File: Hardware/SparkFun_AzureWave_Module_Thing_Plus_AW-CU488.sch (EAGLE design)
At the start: 59 parts, among them J1 THING_PLUS, J3 QWIIC_RA, J5 USB-C, Q1 3.1A/30V/105mΩ, Q2 MBT3904DW1T1, U2 CP210X, U3 AP2112K-3.3V, U4 MCP73831

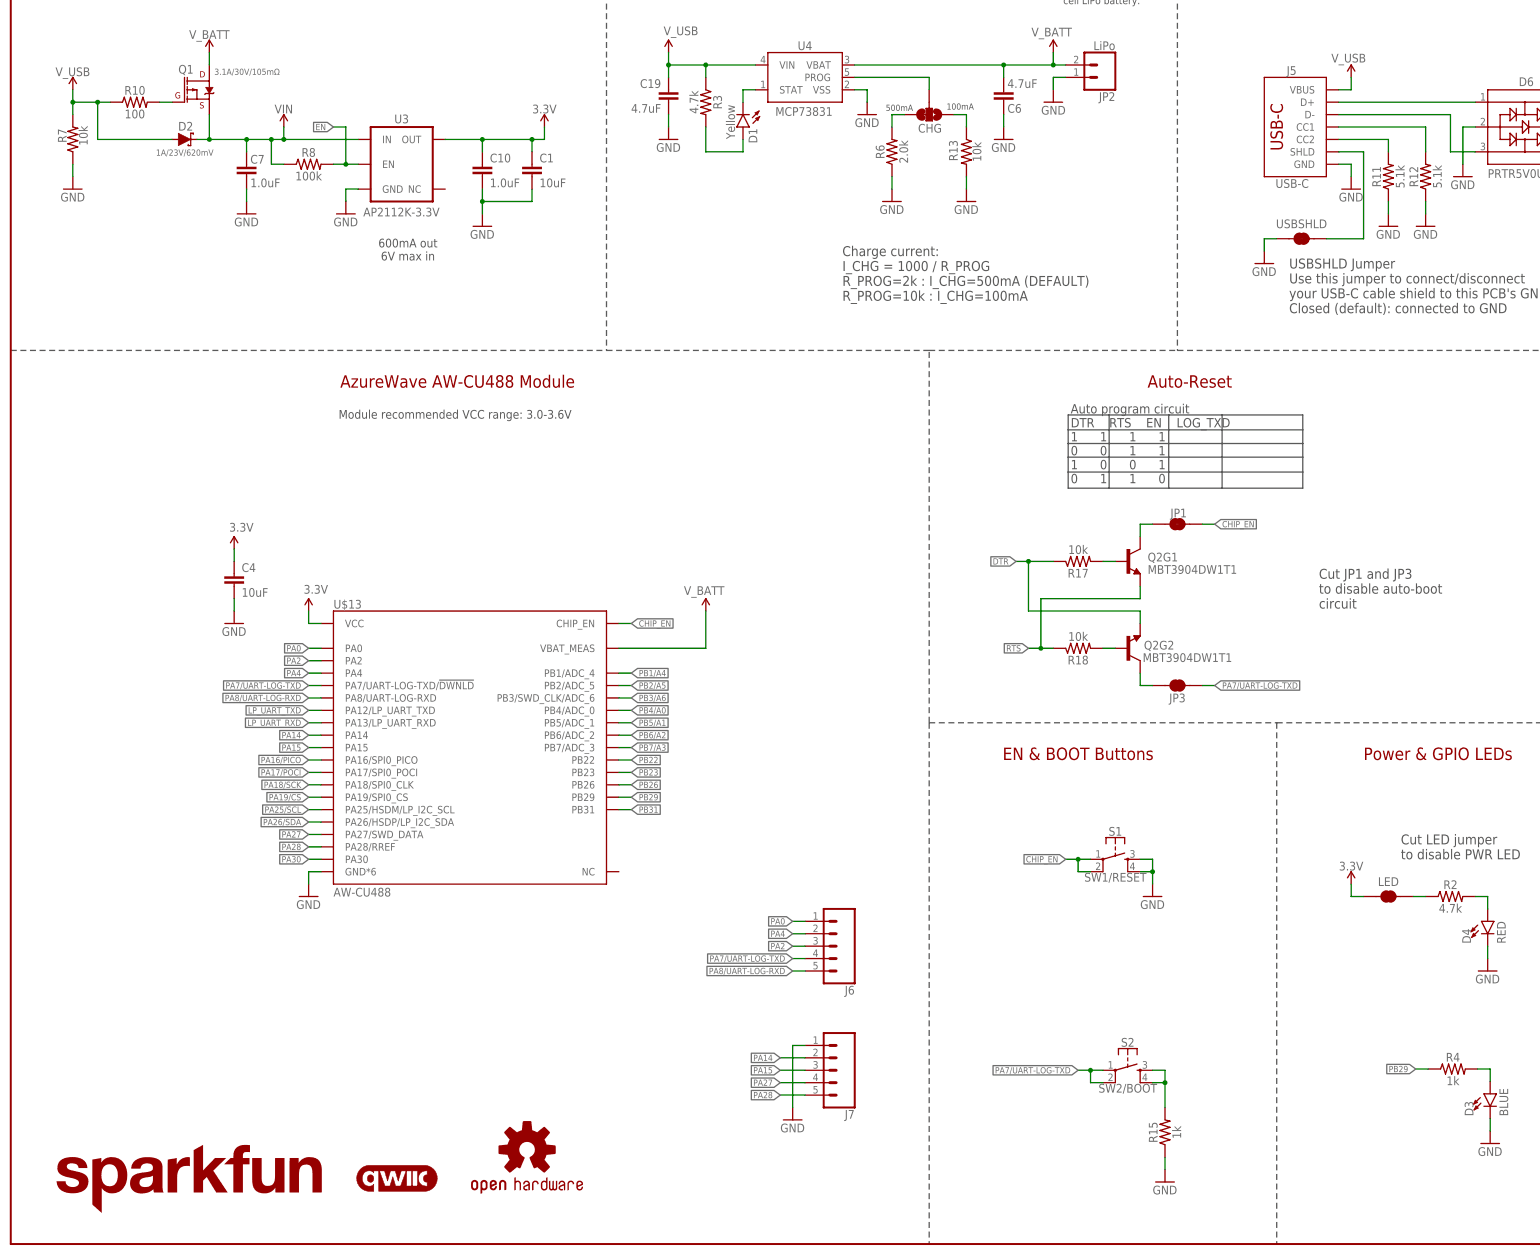
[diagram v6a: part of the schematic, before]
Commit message: more changes from reds review
-auto-reset disable jumpers changed to JP1 and JP2
-added more measures to top pht header on header rows
-swapped vreg from ap2112 to XC6222
-Add SFE LOGO to bottom silk
-more gnd vias near potential gnd loops
-fixed acid traps
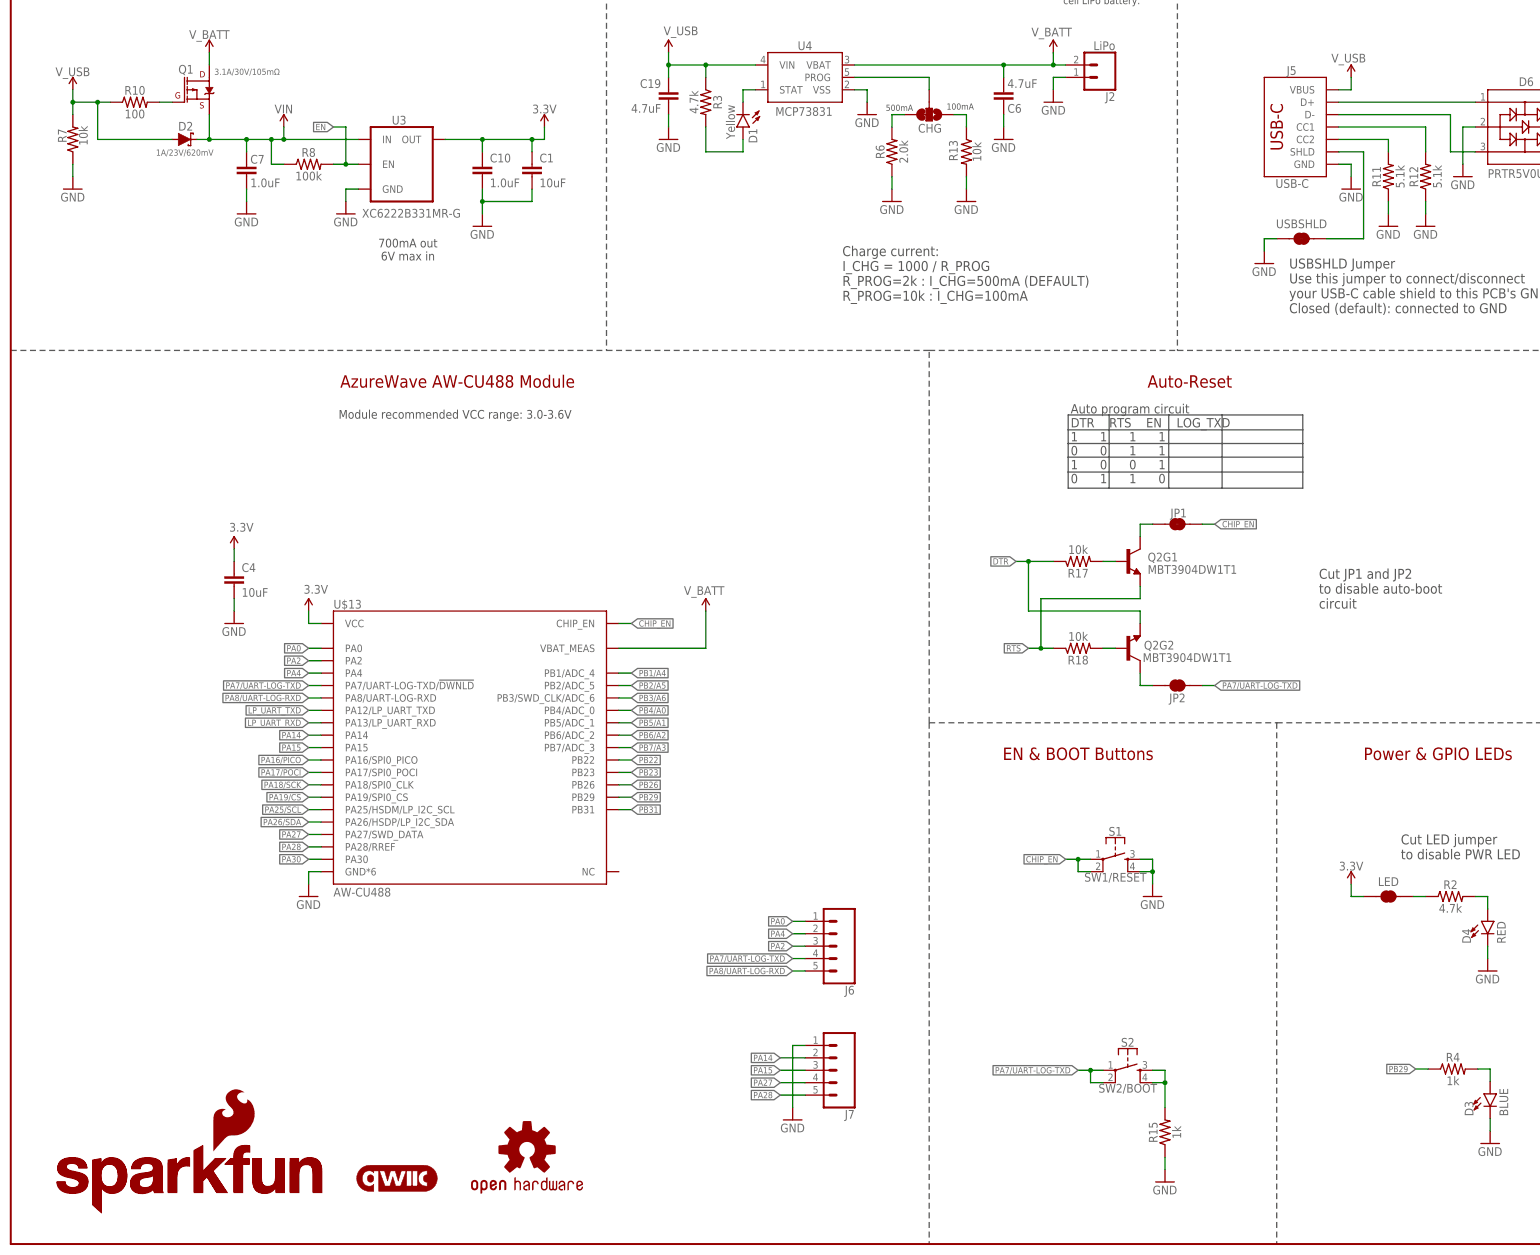
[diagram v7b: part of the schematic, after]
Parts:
- removed JP3: JUMPER-SMT_2_NC_TRACE_SILK, SparkFun-Jumpers:JUMPER-SMT_2_NC_TRACE_SILK
- added J2: LiPo, SparkFun-Connectors:CONN_02-JST-2MM-SMT
- added LOGO3: SFE_LOGO_NAME_FLAME.1_INCH, SparkFun-Aesthetics:SFE_LOGO_NAME_FLAME.1_INCH
- JP2: value LiPo -> JUMPER-SMT_2_NC_TRACE_SILK; device SparkFun-Connectors:CONN_02-JST-2MM-SMT -> SparkFun-Jumpers:JUMPER-SMT_2_NC_TRACE_SILK
- U3: value AP2112K-3.3V -> XC6222B331MR-G; device SparkFun-IC-Power:V_REG_AP2112K-3.3V -> SparkFun-IC-Power:XC6222B331MR-G
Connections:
- net GND: now also J2.2; no longer JP2.2
- net N$10: now also JP2.1; no longer JP3.1
- net PA7/UART-LOG-TXD: now also JP2.2; no longer JP3.2
- net V_BATT: now also J2.1; no longer JP2.1
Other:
- note added: "700mA out 6V max in"
- note added: "Cut JP1 and JP2 to disable auto-boot circuit"
- note removed: "600mA out 6V max in"
- note removed: "Cut JP1 and JP3 to disable auto-boot circuit"
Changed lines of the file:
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@@
 <part name="R7" library="SparkFun-Resistors" deviceset="10KOHM" device="-0402T-1/16W-1%" value="10k"/>
 <part name="GND13" library="SparkFun-PowerSymbols" deviceset="GND" device=""/>
-<part name="JP2" library="SparkFun-Connectors" deviceset="CONN_02" device="-JST-2MM-SMT" value="LiPo"/>
+<part name="J2" library="SparkFun-Connectors" deviceset="CONN_02" device="-JST-2MM-SMT" value="LiPo"/>
 <part name="GND4" library="SparkFun-PowerSymbols" deviceset="GND" device=""/>
 <part name="D1" library="SparkFun-LED" deviceset="LED-YELLOW" device="0603" value="Yellow"/>
 <part name="R3" library="SparkFun-Resistors" deviceset="4.7KOHM" device="-0402T-1/16W-1%" value="4.7k"/>
-<part name="U3" library="SparkFun-IC-Power" deviceset="V_REG_AP2112" device="K-3.3V" value="AP2112K-3.3V">
+<part name="U3" library="SparkFun-IC-Power" deviceset="XC6222" device="B331MR-G" value="XC6222B331MR-G">
 <attribute name="PROD_ID" value="VREG-12457"/>
 </part>
@@
 <part name="GND22" library="SparkFun-PowerSymbols" deviceset="GND" device=""/>
 <part name="JP1" library="SparkFun-Jumpers" deviceset="JUMPER-SMT_2_NC_TRACE" device="_SILK" package3d_urn="urn:adsk.eagle:package:39281/1" value=""/>
-<part name="JP3" library="SparkFun-Jumpers" deviceset="JUMPER-SMT_2_NC_TRACE" device="_SILK" package3d_urn="urn:adsk.eagle:package:39281/1" value=""/>
+<part name="JP2" library="SparkFun-Jumpers" deviceset="JUMPER-SMT_2_NC_TRACE" device="_SILK" package3d_urn="urn:adsk.eagle:package:39281/1" value=""/>
 <part name="LOGO1" library="SparkFun-Aesthetics" deviceset="SFE_LOGO_NAME" device=".1_INCH"/>
+<part name="LOGO3" library="SparkFun-Aesthetics" deviceset="SFE_LOGO_NAME_FLAME" device=".1_INCH"/>
 </parts>
 <sheets>
@@
 <text x="60.96" y="271.78" size="2.54" layer="94" font="vector" align="bottom-center">Voltage Regulator</text>
 <text x="177.8" y="271.78" size="2.54" layer="94" font="vector" align="bottom-center">Lithium-Polymer Battery Charger (1-cell)</text>
-<text x="81.28" y="205.74" size="1.778" layer="97" font="vector" align="top-center">600mA out
+<text x="81.28" y="205.74" size="1.778" layer="97" font="vector" align="top-center">700mA out
 6V max in</text>
 <wire x1="0" y1="182.88" x2="121.92" y2="182.88" width="0.2032" layer="97" style="longdash"/>
@@
 your USB-C cable shield to this PCB's GND.
 Closed (default): connected to GND</text>
-<text x="267.716" y="130.048" size="2.032" layer="97" font="vector" rot="MR180" align="top-left">Cut JP1 and JP3
+<text x="267.716" y="130.048" size="2.032" layer="97" font="vector" rot="MR180" align="top-left">Cut JP1 and JP2
 to disable auto-boot
 circuit</text>
@@
 <attribute name="VALUE" x="10.16" y="213.36" size="1.778" layer="96" font="vector"/>
 </instance>
-<instance part="JP2" gate="G$1" x="223.52" y="241.3" smashed="yes" rot="R180">
+<instance part="J2" gate="G$1" x="223.52" y="241.3" smashed="yes" rot="R180">
 <attribute name="VALUE" x="226.06" y="246.126" size="1.778" layer="96" font="vector" rot="R180"/>
 <attribute name="NAME" x="226.06" y="235.712" size="1.778" layer="95" font="vector" rot="R180"/>
@@
 <instance part="U3" gate="G$1" x="81.28" y="220.98" smashed="yes">
 <attribute name="PROD_ID" x="81.28" y="220.98" size="1.778" layer="96" display="off"/>
-<attribute name="NAME" x="78.486" y="229.362" size="1.778" layer="95" font="vector"/>
-<attribute name="VALUE" x="72.136" y="210.312" size="1.778" layer="96" font="vector"/>
+<attribute name="NAME" x="77.978" y="229.108" size="1.778" layer="95" font="vector"/>
+<attribute name="VALUE" x="71.882" y="211.836" size="1.778" layer="96" font="vector" align="top-left"/>
 </instance>
 <instance part="Q1" gate="G$1" x="38.1" y="236.22" smashed="yes">
@@
 <attribute name="VALUE" x="238.76" y="144.272" size="1.778" layer="96" font="vector" align="center"/>
 </instance>
-<instance part="JP3" gate="G$1" x="238.76" y="114.3" smashed="yes">
+<instance part="JP2" gate="G$1" x="238.76" y="114.3" smashed="yes">
 <attribute name="NAME" x="238.76" y="111.76" size="1.778" layer="95" font="vector" align="center"/>
 <attribute name="VALUE" x="238.76" y="111.252" size="1.778" layer="96" font="vector" align="center"/>
 </instance>
 <instance part="LOGO1" gate="G$1" x="7.366" y="6.35" smashed="yes"/>
+<instance part="LOGO3" gate="G$1" x="8.636" y="5.842" smashed="yes"/>
 </instances>
 <busses>
@@
 <pinref part="GND4" gate="1" pin="GND"/>
 <wire x1="213.36" y1="238.76" x2="213.36" y2="236.22" width="0.1524" layer="91"/>
-<pinref part="JP2" gate="G$1" pin="2"/>
+<pinref part="J2" gate="G$1" pin="2"/>
 <wire x1="213.36" y1="238.76" x2="215.9" y2="238.76" width="0.1524" layer="91"/>
 </segment>
@@
 <pinref part="U4" gate="G$1" pin="VBAT"/>
 <wire x1="203.2" y1="241.3" x2="172.72" y2="241.3" width="0.1524" layer="91"/>
-<pinref part="JP2" gate="G$1" pin="1"/>
+<pinref part="J2" gate="G$1" pin="1"/>
 <wire x1="213.36" y1="241.3" x2="215.9" y2="241.3" width="0.1524" layer="91"/>
 </segment>
@@
 <label x="246.38" y="114.3" size="1.27" layer="95" font="vector" rot="MR180" xref="yes"/>
 <wire x1="243.84" y1="114.3" x2="246.38" y2="114.3" width="0.1524" layer="91"/>
-<pinref part="JP3" gate="G$1" pin="2"/>
+<pinref part="JP2" gate="G$1" pin="2"/>
 </segment>
 </net>
@@
 <net name="N$10" class="0">
 <segment>
-<pinref part="JP3" gate="G$1" pin="1"/>
+<pinref part="JP2" gate="G$1" pin="1"/>
 <wire x1="233.68" y1="114.3" x2="231.14" y2="114.3" width="0.1524" layer="91"/>
 <pinref part="Q2" gate="G2" pin="C"/>

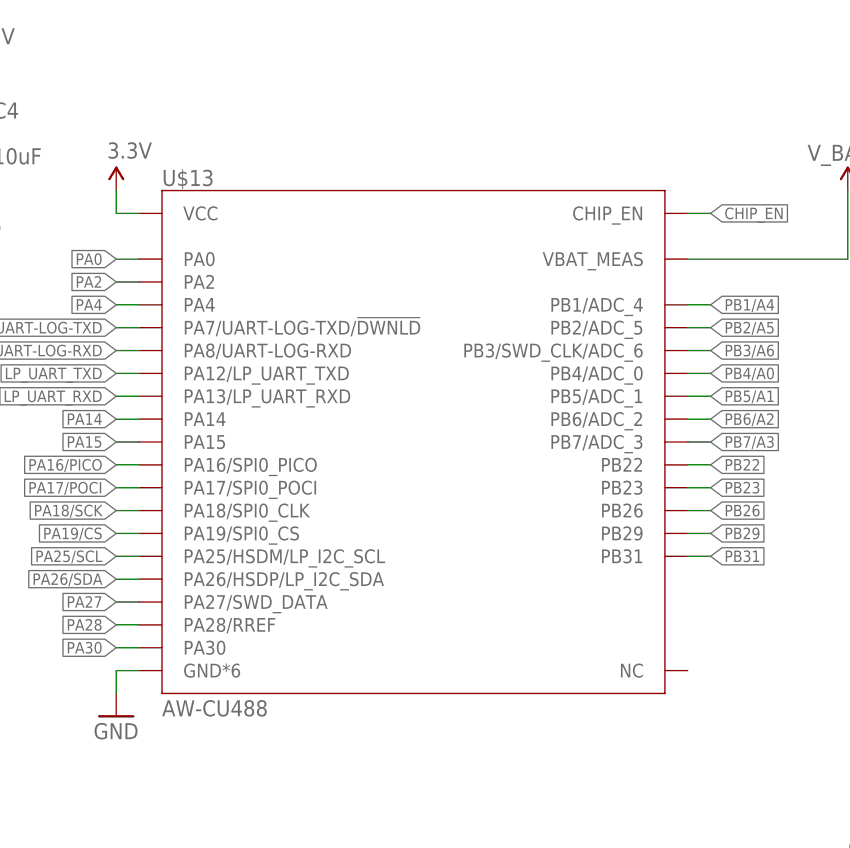
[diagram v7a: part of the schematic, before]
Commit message: AW-CU488 library work
-removed NC pin
-took "$" out of part name attribute
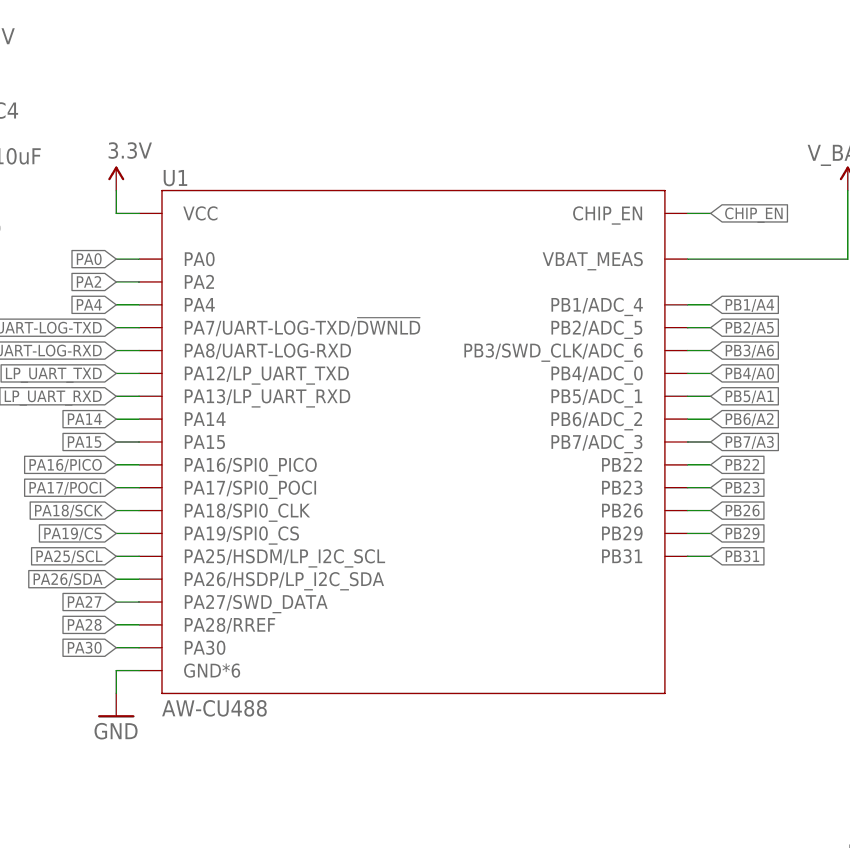
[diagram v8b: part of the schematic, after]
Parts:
- removed U$13: AW-CU488, temp:AW-CU488LGA150
- added U1: AW-CU488, temp:AW-CU488LGA150
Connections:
- net 3.3V: now also U1.VCC; no longer U$13.VCC
- net CHIP_EN: now also U1.CHIP_EN; no longer U$13.CHIP_EN
- net GND: now also U1.GND*6; no longer U$13.GND*6
- net LP_UART_RXD: now also U1.PA13/LP_UART_RXD; no longer U$13.PA13/LP_UART_RXD
- net LP_UART_TXD: now also U1.PA12/LP_UART_TXD; no longer U$13.PA12/LP_UART_TXD
- net PA0: now also U1.PA0; no longer U$13.PA0
- net PA14: now also U1.PA14; no longer U$13.PA14
- net PA15: now also U1.PA15; no longer U$13.PA15
- net PA16/PICO: now also U1.PA16/SPI0_PICO; no longer U$13.PA16/SPI0_PICO
- net PA17/POCI: now also U1.PA17/SPI0_POCI; no longer U$13.PA17/SPI0_POCI
- net PA18/SCK: now also U1.PA18/SPI0_CLK; no longer U$13.PA18/SPI0_CLK
- net PA19/CS: now also U1.PA19/SPI0_CS; no longer U$13.PA19/SPI0_CS
- net PA2: now also U1.PA2; no longer U$13.PA2
- net PA25/SCL: now also U1.PA25/HSDM/LP_I2C_SCL; no longer U$13.PA25/HSDM/LP_I2C_SCL
- net PA26/SDA: now also U1.PA26/HSDP/LP_I2C_SDA; no longer U$13.PA26/HSDP/LP_I2C_SDA
- net PA27: now also U1.PA27/SWD_DATA; no longer U$13.PA27/SWD_DATA
- net PA28: now also U1.PA28/RREF; no longer U$13.PA28/RREF
- net PA30: now also U1.PA30; no longer U$13.PA30
- net PA4: now also U1.PA4; no longer U$13.PA4
- net PA7/UART-LOG-TXD: now also U1.PA7/UART-LOG-TXD/!DWNLD!; no longer U$13.PA7/UART-LOG-TXD/!DWNLD!
- net PA8/UART-LOG-RXD: now also U1.PA8/UART-LOG-RXD; no longer U$13.PA8/UART-LOG-RXD
- net PB1/A4: now also U1.PB1/ADC_4; no longer U$13.PB1/ADC_4
- net PB2/A5: now also U1.PB2/ADC_5; no longer U$13.PB2/ADC_5
- net PB22: now also U1.PB22; no longer U$13.PB22
- net PB23: now also U1.PB23; no longer U$13.PB23
- net PB26: now also U1.PB26; no longer U$13.PB26
- net PB29: now also U1.PB29; no longer U$13.PB29
- net PB3/A6: now also U1.PB3/SWD_CLK/ADC_6; no longer U$13.PB3/SWD_CLK/ADC_6
- net PB31: now also U1.PB31; no longer U$13.PB31
- net PB4/A0: now also U1.PB4/ADC_0; no longer U$13.PB4/ADC_0
- net PB5/A1: now also U1.PB5/ADC_1; no longer U$13.PB5/ADC_1
- net PB6/A2: now also U1.PB6/ADC_2; no longer U$13.PB6/ADC_2
- net PB7/A3: now also U1.PB7/ADC_3; no longer U$13.PB7/ADC_3
- net V_BATT: now also U1.VBAT_MEAS; no longer U$13.VBAT_MEAS
